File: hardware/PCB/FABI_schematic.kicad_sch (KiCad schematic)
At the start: 61 parts, among them J1 AudioJack3_Ground, J1 Conn_01x04_Male, J10 Conn_01x03_Male, J11 display_connector_91601-304LF, J11_GND1 Conn_01x01_Male, J11_VDD1 Conn_01x01_Male, J11_data1 Conn_01x01_Male, J2 AudioJack3_Ground, J3 AudioJack3_Ground, J4 AudioJack3_Ground, J5 AudioJack3_Ground, J6 009159005551906, J6 AudioJack3_Ground, J9 Conn_ARM_SWD_TagConnect_TC2030, Q2 BSS806, U1 MIC5504-3.3YM5, U1 RaspberryPi_Pico_W_SecondaryP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, U2 TPD3E001DRLR, U4 TPD3E001DRLR, U4 TSOP4838, U6 TPD3E001DRLR, U7 TPD3E001DRLR

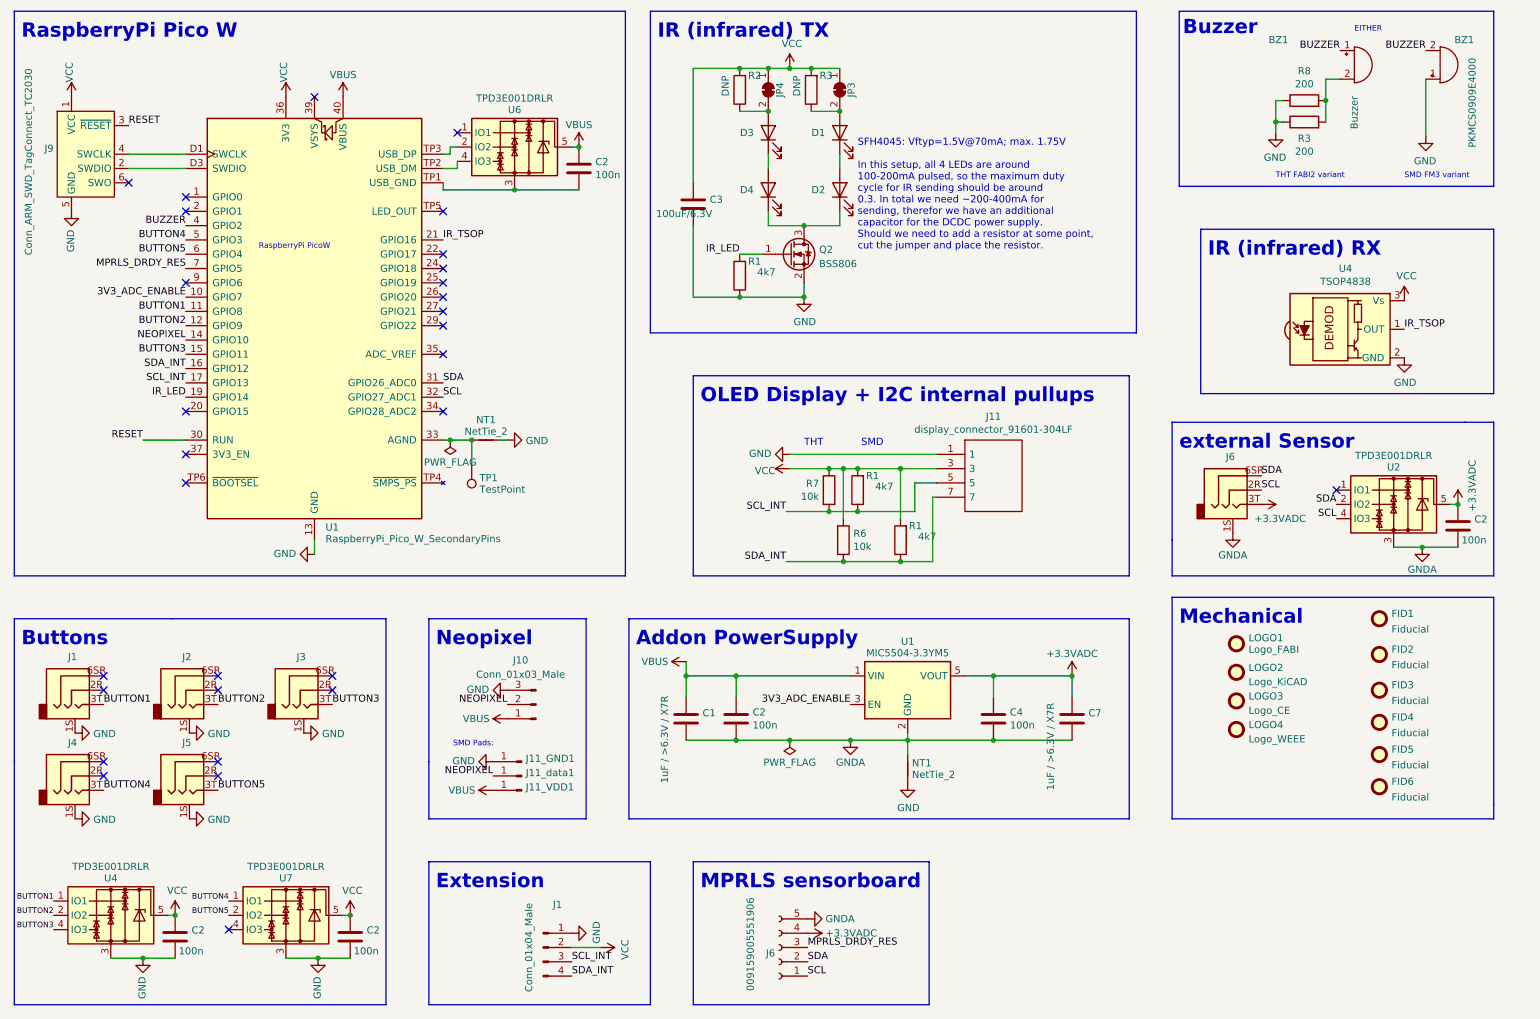
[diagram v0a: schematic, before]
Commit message: Changed TVS array to a bigger one, cleaned up libraries
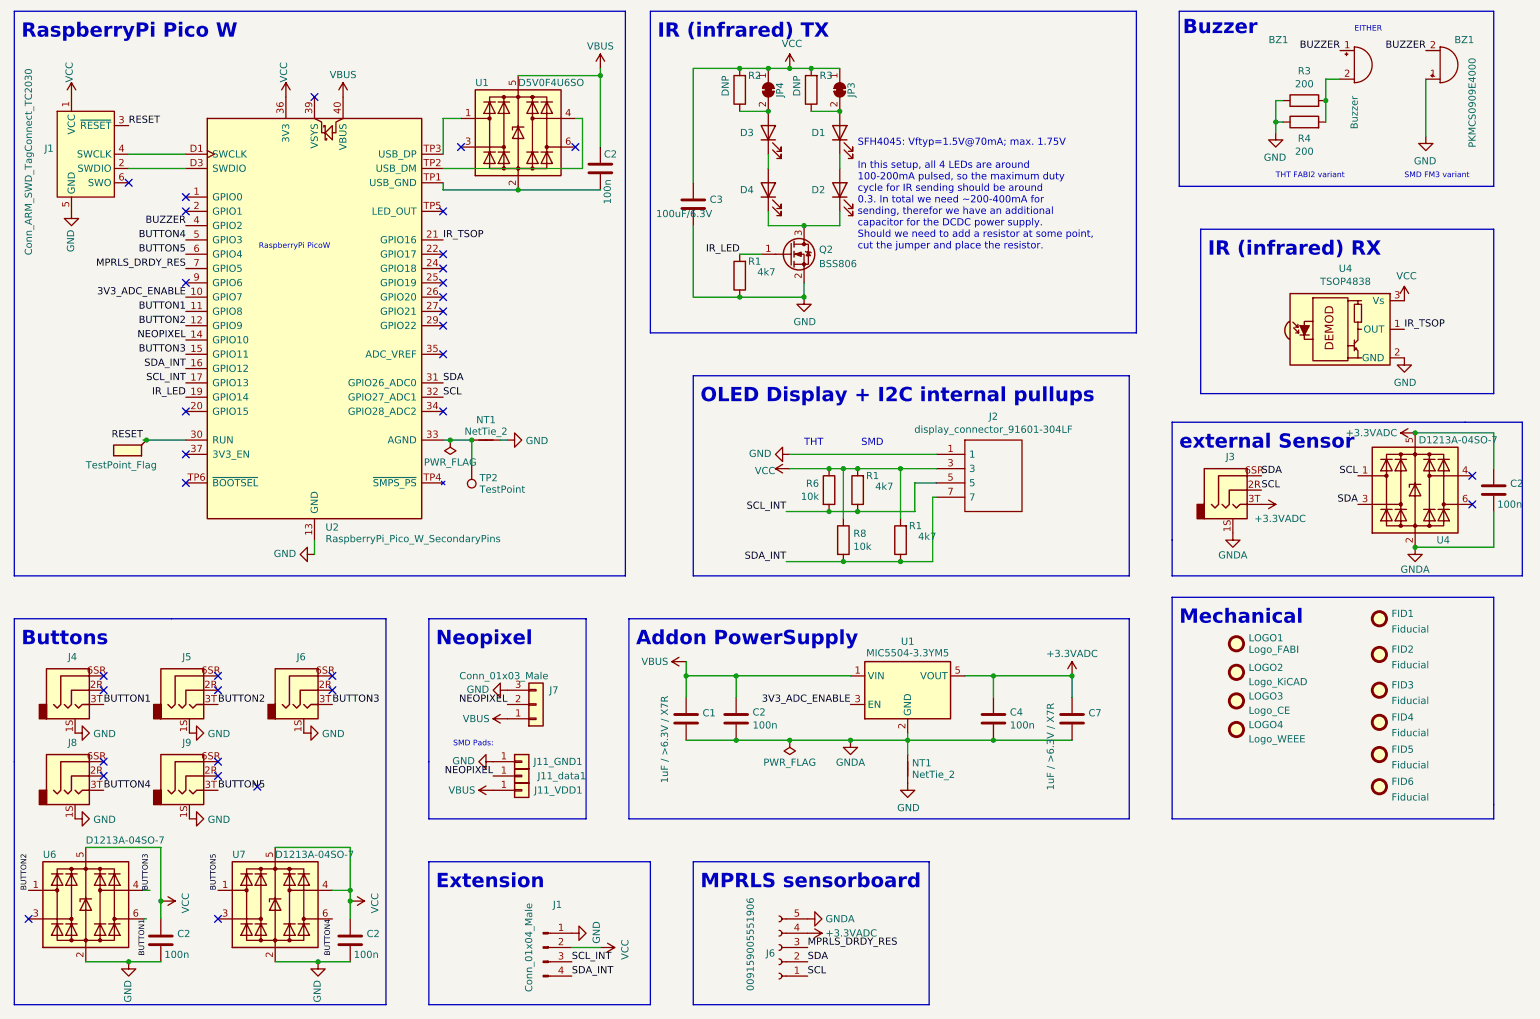
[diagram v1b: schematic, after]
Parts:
- removed U2, U4, U6, U7: TPD3E001DRLR, Package_TO_SOT_SMD:SOT-553, symbol Power_Protection:TPD3E001DRLR
- added TP1: TestPoint_Flag, symbol Connector:TestPoint_Flag
- added U1: D5V0F4U6SO, Package_SO:SC-74-6_1.5x2.9mm_P0.95mm, symbol Power_Protection:WE-TVS-824015043
- added U4, U6, U7: D1213A-04SO-7, Package_SO:SC-74-6_1.5x2.9mm_P0.95mm, symbol Power_Protection:WE-TVS-824015043
- J11_GND1, J11_VDD1, J11_data1: symbol FABI_schematic-rescue:Conn_01x01_Male-Connector -> Connector_Generic:Conn_01x01
- J7: renamed from J10; symbol FABI_schematic-rescue:Conn_01x03_Male-Connector -> Connector_Generic:Conn_01x03; now in the parts list
- renumbered J9 to J1, J11 to J2, J6 to J3, J1 to J4, J2 to J5, J3 to J6, J4 to J8, J5 to J9, R8 to R3, R3 to R4, R7 to R6, R6 to R8, TP1 to TP2, U1 to U2
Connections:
- net +3.3VADC: now also U4.5 (VBUS)
- net BUTTON1: now also U6.6 (I/O4)
- net BUTTON2: now also U6.1 (I/O1)
- net BUTTON3: now also U6.4 (I/O3)
- net BUTTON4: now also U7.6 (I/O4)
- net BUTTON5: now also U7.1 (I/O1)
- net GND: now also U6.2 (GND), U7.2 (GND)
- net GNDA: now also U4.2 (GND)
- net RESET: now also TP1.1
- net SCL: now also U4.1 (I/O1)
- net SDA: now also U4.3 (I/O2)
- net VBUS: now also U1.5 (VBUS)
- net VCC: now also U6.5 (VBUS), U7.4 (I/O3), U7.5 (VBUS)
- net at C2.2, U2.TP1 (USB_GND): now also U1.2 (GND)
- net at U2.TP3 (USB_DP): now also U1.1 (I/O1)
- net at U2.TP2 (USB_DM): now also U1.4 (I/O3)
- no-connect marks 30 -> 34
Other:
- moved on the sheet: C2, J11_GND1, J11_VDD1, J11_data1

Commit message: Changed footprint in SCH as well
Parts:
- J11_GND1, J11_VDD1, J11_data1: footprint Connector_Wire:SolderWirePad_1x01_SMD_1x2mm -> FABI:SolderWirePad_1x01_SMD_1x2mm_NOPASTE
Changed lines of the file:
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@@
       (effects (font (size 1.27 1.27)) (justify right) hide)
     )
-    (property "Footprint" "Connector_Wire:SolderWirePad_1x01_SMD_1x2mm" (at 104.14 153.67 0)
+    (property "Footprint" "FABI:SolderWirePad_1x01_SMD_1x2mm_NOPASTE" (at 104.14 153.67 0)
       (effects (font (size 1.27 1.27)) hide)
     )
@@
       (effects (font (size 1.27 1.27)) (justify right) hide)
     )
-    (property "Footprint" "Connector_Wire:SolderWirePad_1x01_SMD_1x2mm" (at 104.14 156.21 0)
+    (property "Footprint" "FABI:SolderWirePad_1x01_SMD_1x2mm_NOPASTE" (at 104.14 156.21 0)
       (effects (font (size 1.27 1.27)) hide)
     )
@@
       (effects (font (size 1.27 1.27)) (justify right) hide)
     )
-    (property "Footprint" "Connector_Wire:SolderWirePad_1x01_SMD_1x2mm" (at 104.14 158.75 0)
+    (property "Footprint" "FABI:SolderWirePad_1x01_SMD_1x2mm_NOPASTE" (at 104.14 158.75 0)
       (effects (font (size 1.27 1.27)) hide)
     )

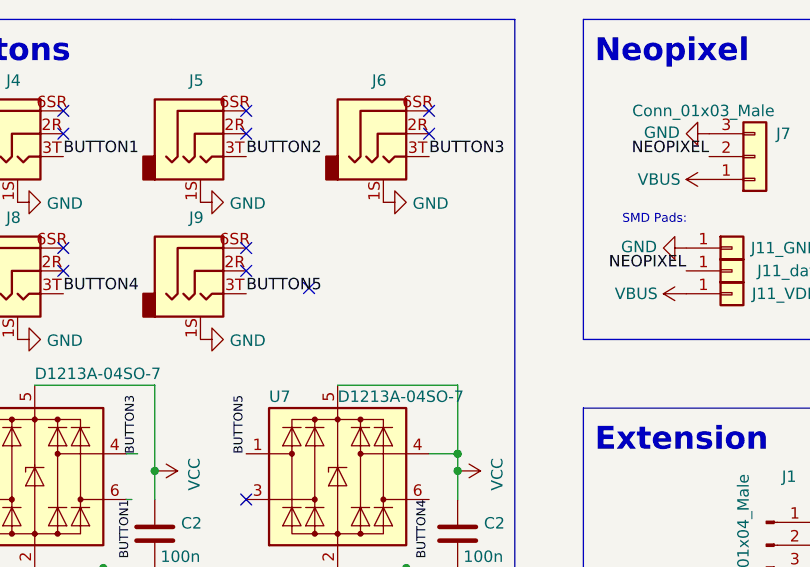
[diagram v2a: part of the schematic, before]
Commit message: Added note on replacement jack plugs & added iBOM
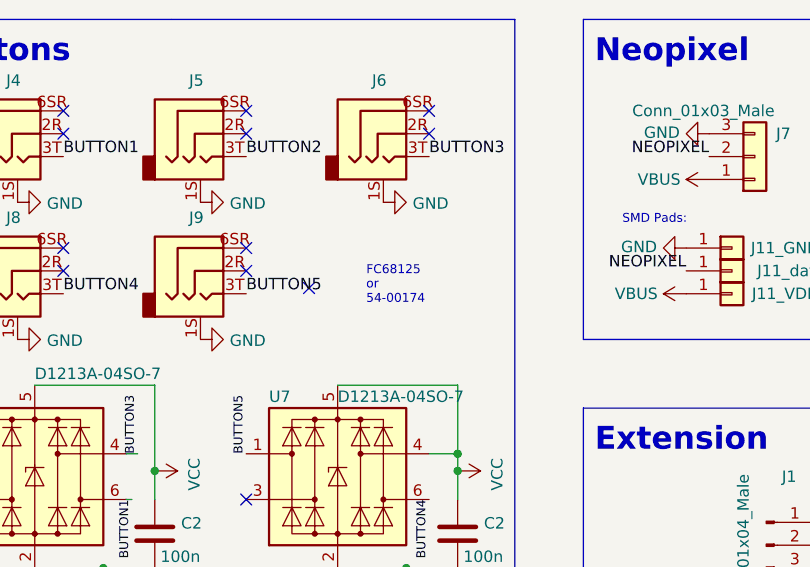
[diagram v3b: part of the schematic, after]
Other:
- note added: "FC68125 or 54-00174"
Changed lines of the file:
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@@
     (effects (font (size 2.54 2.54) (thickness 0.508) bold) (justify left bottom))
+  )
+  (text "FC68125\nor\n54-00174" (at 63.5 160.02 0)
+    (effects (font (size 0.9906 0.9906)) (justify left bottom))
   )
   (text "Buttons" (at 15.24 133.35 0)

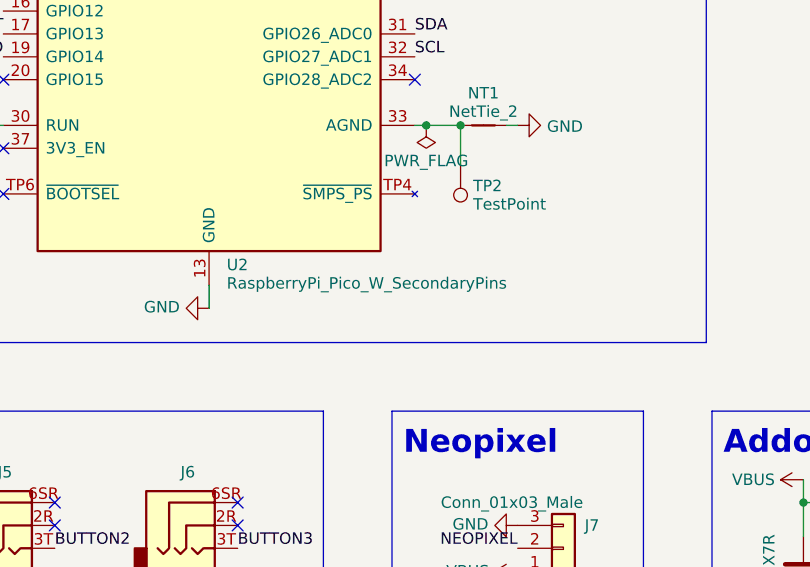
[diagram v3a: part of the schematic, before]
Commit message: Adapted BOM in SCH; added new ConstructionManual PDF
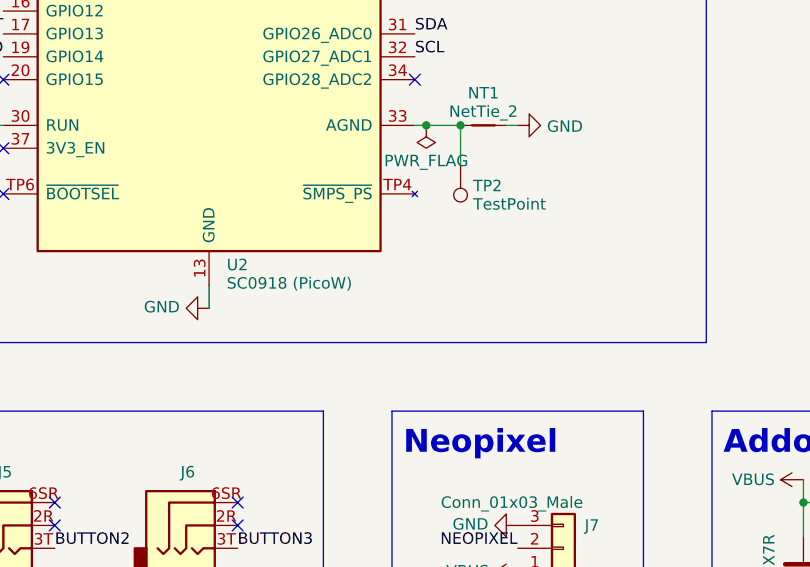
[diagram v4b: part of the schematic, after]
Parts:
- J3, J4, J5, J6, J8, J9: value AudioJack3_Ground -> 54-00174 / FC68125; Digikey (none) -> 839-54-00174CT-ND
- J7: Digikey (none) -> DNP; Farnell (none) -> DNP
- U1: Digikey (none) -> D5V0F4U6SO-7DICT-ND
- U2: value RaspberryPi_Pico_W_SecondaryPins -> SC0918 (PicoW); Digikey (none) -> 2648-SC0918CT-ND
- U4, U6, U7: Digikey (none) -> D1213A-04SO-7DICT-ND
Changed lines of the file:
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@@
       (effects (font (size 1.27 1.27)) hide)
     )
+    (property "Digikey" "DNP" (at 106.68 143.51 0)
+      (effects (font (size 1.27 1.27)) hide)
+    )
+    (property "Farnell" "DNP" (at 106.68 143.51 0)
+      (effects (font (size 1.27 1.27)) hide)
+    )
     (pin "1")
     (pin "2")
@@
       (effects (font (size 1.27 1.27)) hide)
     )
+    (property "Description" "note: deprecated THT buzzer" (at 252.095 29.845 0)
+      (effects (font (size 1.27 1.27)) hide)
+    )
     (pin "1")
     (pin "2")
@@
       (effects (font (size 1.27 1.27)) (justify left) hide)
     )
-    (property "Description" "Dubox 2.54mm, Board to Board Connector, PCB Mounted Receptacle, Vertical , Surface Mount, Dual Entry ,Single row , 4 Positions, 2.54mm (0.100in) Pitch" (at 208.28 102.87 0)
+    (property "Description" "" (at 208.28 102.87 0)
       (effects (font (size 1.27 1.27)) (justify left) hide)
     )
@@
       (effects (font (size 1.27 1.27)))
     )
-    (property "Value" "AudioJack3_Ground" (at 24.3078 135.0264 0)
+    (property "Value" "54-00174 / FC68125" (at 24.3078 135.0264 0)
       (effects (font (size 1.27 1.27)) hide)
     )
@@
       (effects (font (size 1.27 1.27)) hide)
     )
+    (property "Digikey" "839-54-00174CT-ND" (at 24.765 140.97 0)
+      (effects (font (size 1.27 1.27)) hide)
+    )
     (pin "1S")
     (pin "2R")
@@
       (effects (font (size 1.27 1.27)) hide)
     )
+    (property "Digikey" "D1213A-04SO-7DICT-ND" (at 60.325 179.07 0)
+      (effects (font (size 1.27 1.27)) hide)
+    )
     (pin "1")
     (pin "2")
@@
       (effects (font (size 1.27 1.27)) hide)
     )
+    (property "Digikey" "D1213A-04SO-7DICT-ND" (at 262.89 105.41 0)
+      (effects (font (size 1.27 1.27)) hide)
+    )
     (pin "1")
     (pin "2")
@@
       (effects (font (size 1.27 1.27)))
     )
-    (property "Value" "AudioJack3_Ground" (at 44.6278 150.2664 0)
+    (property "Value" "54-00174 / FC68125" (at 44.6278 150.2664 0)
       (effects (font (size 1.27 1.27)) hide)
     )
@@
       (effects (font (size 1.27 1.27)) hide)
     )
+    (property "Digikey" "839-54-00174CT-ND" (at 45.085 156.21 0)
+      (effects (font (size 1.27 1.27)) hide)
+    )
     (pin "1S")
     (pin "2R")
@@
       (effects (font (size 1.27 1.27)) (justify left))
     )
-    (property "Value" "RaspberryPi_Pico_W_SecondaryPins" (at 69.2659 114.07 0)
+    (property "Value" "SC0918 (PicoW)" (at 69.2659 114.07 0)
       (effects (font (size 1.27 1.27)) (justify left))
     )
@@
       (effects (font (size 1.27 1.27)) hide)
     )
+    (property "Digikey" "2648-SC0918CT-ND" (at 67.31 76.2 0)
+      (effects (font (size 1.27 1.27)) hide)
+    )
     (pin "1")
     (pin "10")
@@
       (effects (font (size 1.27 1.27)))
     )
-    (property "Value" "AudioJack3_Ground" (at 64.9478 135.0264 0)
+    (property "Value" "54-00174 / FC68125" (at 64.9478 135.0264 0)
       (effects (font (size 1.27 1.27)) hide)
     )
@@
       (effects (font (size 1.27 1.27)) hide)
     )
+    (property "Digikey" "839-54-00174CT-ND" (at 65.405 140.97 0)
+      (effects (font (size 1.27 1.27)) hide)
+    )
     (pin "1S")
     (pin "2R")
@@
       (effects (font (size 1.27 1.27)))
     )
-    (property "Value" "AudioJack3_Ground" (at 44.6278 135.0264 0)
+    (property "Value" "54-00174 / FC68125" (at 44.6278 135.0264 0)
       (effects (font (size 1.27 1.27)) hide)
     )
@@
       (effects (font (size 1.27 1.27)) hide)
     )
+    (property "Digikey" "839-54-00174CT-ND" (at 45.085 140.97 0)
+      (effects (font (size 1.27 1.27)) hide)
+    )
     (pin "1S")
     (pin "2R")
@@
       (effects (font (size 1.27 1.27)))
     )
-    (property "Value" "AudioJack3_Ground" (at 230.0478 99.4664 0)
+    (property "Value" "54-00174 / FC68125" (at 230.0478 99.4664 0)
       (effects (font (size 1.27 1.27)) hide)
     )
@@
       (effects (font (size 1.27 1.27)) hide)
     )
+    (property "Digikey" "839-54-00174CT-ND" (at 230.505 105.41 0)
+      (effects (font (size 1.27 1.27)) hide)
+    )
     (pin "1S")
     (pin "2R")
@@
       (effects (font (size 1.27 1.27)) hide)
     )
+    (property "Digikey" "D1213A-04SO-7DICT-ND" (at 26.67 179.07 0)
+      (effects (font (size 1.27 1.27)) hide)
+    )
     (pin "1")
     (pin "2")
@@
       (effects (font (size 1.27 1.27)))
     )
-    (property "Value" "AudioJack3_Ground" (at 24.3078 150.2664 0)
+    (property "Value" "54-00174 / FC68125" (at 24.3078 150.2664 0)
       (effects (font (size 1.27 1.27)) hide)
     )
@@
       (effects (font (size 1.27 1.27)) hide)
     )
+    (property "Digikey" "839-54-00174CT-ND" (at 24.765 156.21 0)
+      (effects (font (size 1.27 1.27)) hide)
+    )
     (pin "1S")
     (pin "2R")
@@
       (effects (font (size 1.27 1.27)) hide)
     )
+    (property "Digikey" "D5V0F4U6SO-7DICT-ND" (at 103.505 41.91 0)
+      (effects (font (size 1.27 1.27)) hide)
+    )
